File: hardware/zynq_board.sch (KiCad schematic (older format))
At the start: 0 parts

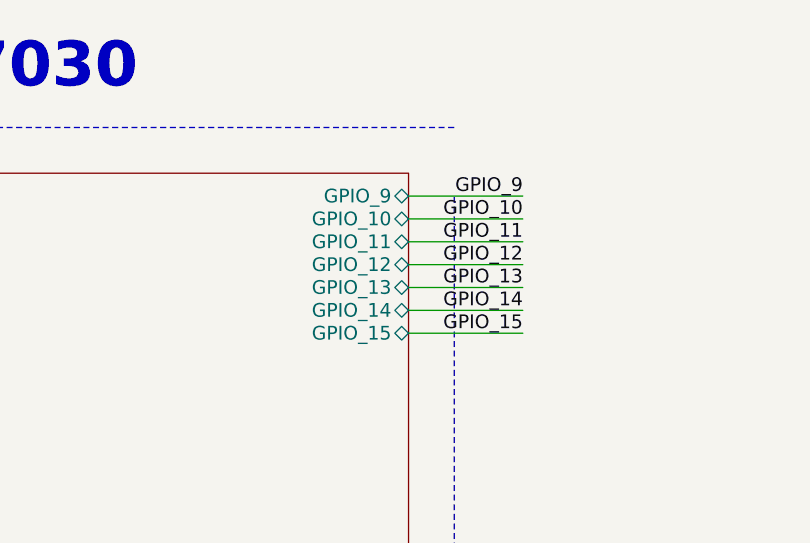
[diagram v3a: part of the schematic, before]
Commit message: general routing mainly power distribution, fixed some footprints
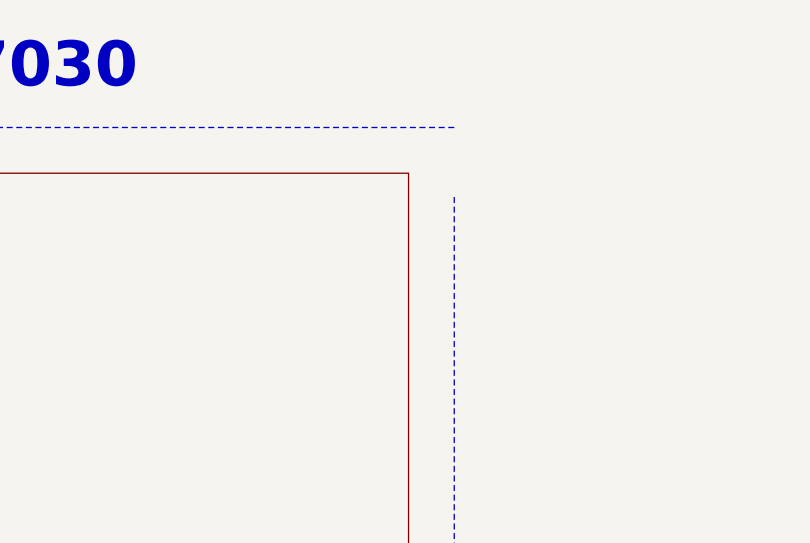
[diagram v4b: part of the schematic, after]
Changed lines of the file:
@@
 Text Label 17150 3800 2    60   ~ 0
 TRIG_IN_3
-Text Label 13750 3250 2    60   ~ 0
-GPIO_15
-Text Label 13750 3150 2    60   ~ 0
-GPIO_14
-Text Label 13750 3050 2    60   ~ 0
-GPIO_13
-Text Label 13750 2950 2    60   ~ 0
-GPIO_12
-Text Label 13750 2850 2    60   ~ 0
-GPIO_11
-Text Label 13750 2750 2    60   ~ 0
-GPIO_10
-Text Label 13750 2650 2    60   ~ 0
-GPIO_9
 Wire Notes Line
 	7250 2350 7250 21950
@@
 Wire Wire Line
 	16400 3800 17150 3800
-Wire Wire Line
-	13250 2650 13750 2650
-Wire Wire Line
-	13250 2750 13750 2750
-Wire Wire Line
-	13250 2850 13750 2850
-Wire Wire Line
-	13250 2950 13750 2950
-Wire Wire Line
-	13250 3050 13750 3050
-Wire Wire Line
-	13250 3150 13750 3150
-Wire Wire Line
-	13250 3250 13750 3250
 Text Label 13750 11150 2    60   ~ 0
 LED1
@@
 F0 "10G Clock" 60
 F1 "10G_clock.sch" 60
-$EndSheet
-$Sheet
-S 10500 2550 2750 3550
-U 596E75FA
-F0 "PL: Bank 34" 60
-F1 "zynq_pl_34.sch" 60
-F2 "SFP_GPIO_18" O R 13250 5400 60
-F3 "RX_LOS_18" I R 13250 5500 60
-F4 "MODDET_18" I R 13250 5600 60
-F5 "SFP_SDA_18" B R 13250 5700 60
-F6 "SFP_SCL_18" B R 13250 5800 60
-F7 "TX_FAULT_18" I R 13250 5900 60
-F8 "TX_DISABLE_18" O R 13250 6000 60
-F9 "ST" O R 13250 5100 60
-F10 "LS_OK_IN_A" O R 13250 5000 60
-F11 "LS_OK_OUT_A" I R 13250 4900 60
-F12 "PRBSEN" O R 13250 4800 60
-F13 "MDC" O R 13250 4700 60
-F14 "MDIO" B R 13250 4600 60
-F15 "GPIO_9" B R 13250 2650 60
-F16 "GPIO_10" B R 13250 2750 60
-F17 "GPIO_11" B R 13250 2850 60
-F18 "GPIO_12" B R 13250 2950 60
-F19 "GPIO_13" B R 13250 3050 60
-F20 "GPIO_14" B R 13250 3150 60
-F21 "GPIO_15" B R 13250 3250 60
 $EndSheet
 $Sheet
@@
 F2 "BUTTON1" O R 16700 9850 60
 $EndSheet
+$Sheet
+S 10500 2550 2750 3550
+U 596E75FA
+F0 "PL: Bank 34" 60
+F1 "zynq_pl_34.sch" 60
+F2 "SFP_GPIO_18" O R 13250 5400 60
+F3 "RX_LOS_18" I R 13250 5500 60
+F4 "MODDET_18" I R 13250 5600 60
+F5 "SFP_SDA_18" B R 13250 5700 60
+F6 "SFP_SCL_18" B R 13250 5800 60
+F7 "TX_FAULT_18" I R 13250 5900 60
+F8 "TX_DISABLE_18" O R 13250 6000 60
+F9 "ST" O R 13250 5100 60
+F10 "LS_OK_IN_A" O R 13250 5000 60
+F11 "LS_OK_OUT_A" I R 13250 4900 60
+F12 "PRBSEN" O R 13250 4800 60
+F13 "MDC" O R 13250 4700 60
+F14 "MDIO" B R 13250 4600 60
+$EndSheet
 $EndSCHEMATC

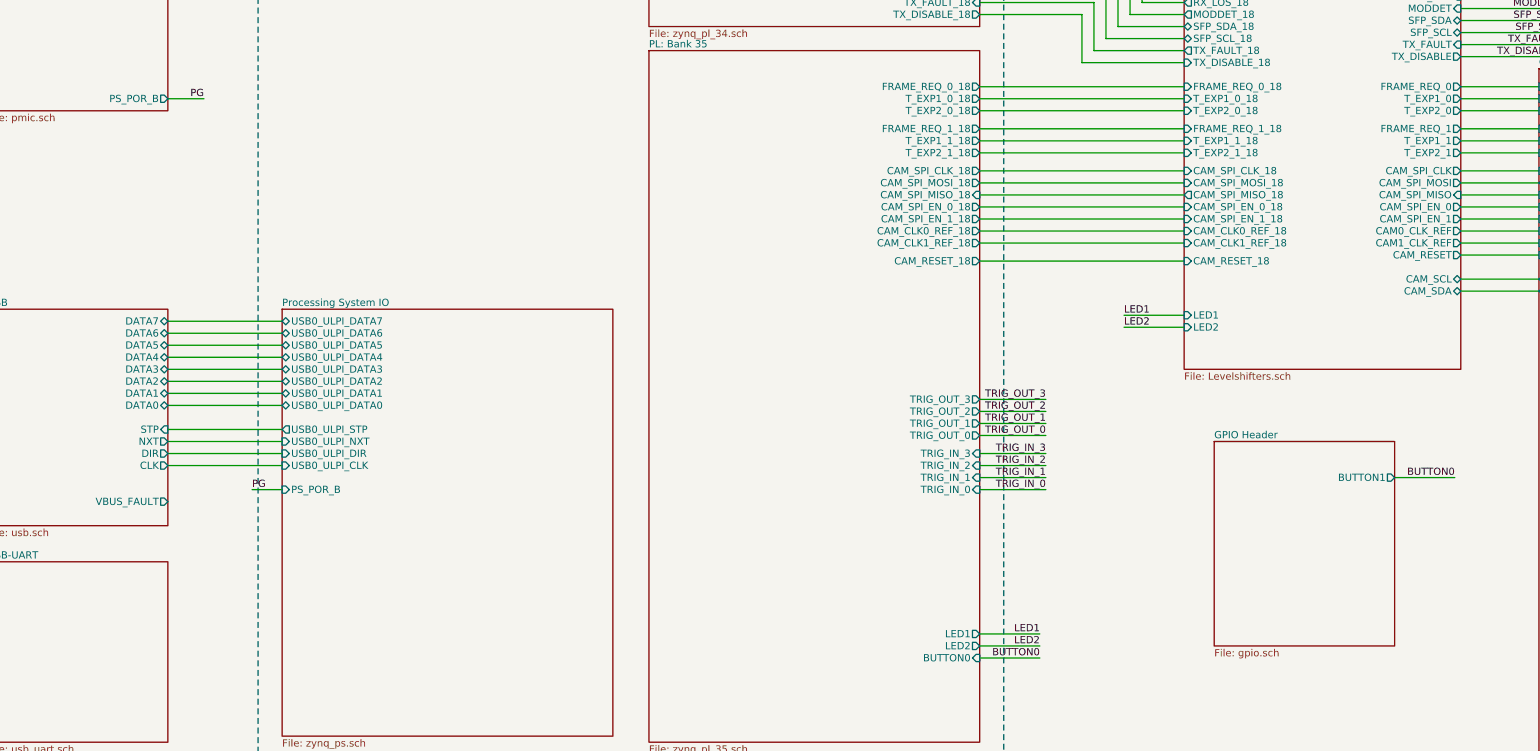
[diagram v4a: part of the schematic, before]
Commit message: First Version without any Net not routed.
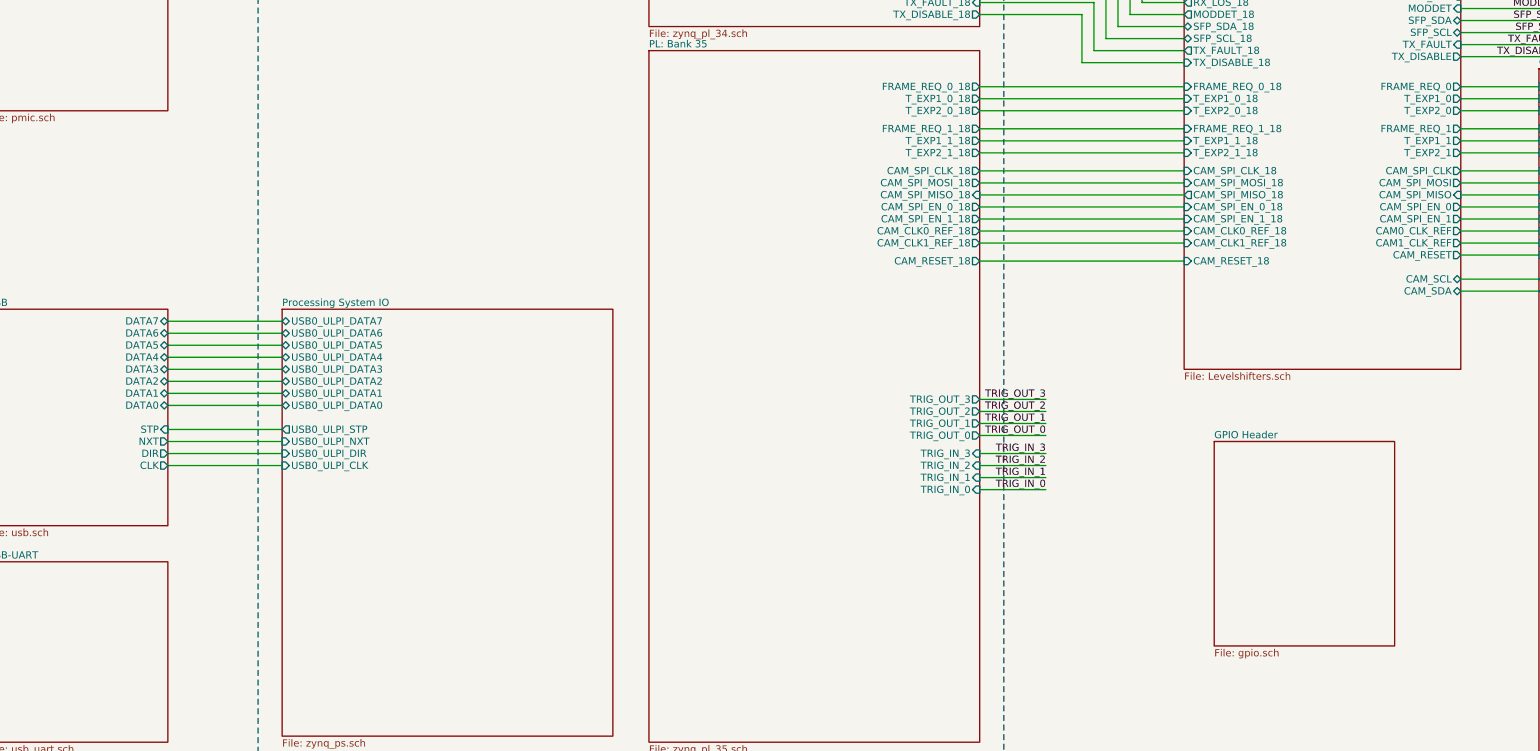
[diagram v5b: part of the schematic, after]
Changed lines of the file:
@@
 F0 "PMIC" 60
 F1 "pmic.sch" 60
-F2 "PS_POR_B" O R 6500 6700 60
 $EndSheet
 $Sheet
@@
 F0 "DDR" 60
 F1 "ddr.sch" 60
-$EndSheet
-$Sheet
-S 5000 8450 1500 1800
-U 5990E90D
-F0 "USB" 60
-F1 "usb.sch" 60
-F2 "DATA7" B R 6500 8550 60
-F3 "DATA6" B R 6500 8650 60
-F4 "DATA5" B R 6500 8750 60
-F5 "DATA4" B R 6500 8850 60
-F6 "DATA3" B R 6500 8950 60
-F7 "DATA2" B R 6500 9050 60
-F8 "DATA1" B R 6500 9150 60
-F9 "DATA0" B R 6500 9250 60
-F10 "STP" I R 6500 9450 60
-F11 "NXT" O R 6500 9550 60
-F12 "DIR" O R 6500 9650 60
-F13 "CLK" O R 6500 9750 60
-F14 "VBUS_FAULT" O R 6500 10050 60
 $EndSheet
 $Sheet
@@
 F44 "CAM_CLK0_REF_18" I L 14950 7800 60
 F45 "CAM0_CLK_REF" O R 17250 7800 60
-F46 "LED1" I L 14950 8500 60
-F47 "LED2" I L 14950 8600 60
 $EndSheet
 $Sheet
@@
 Wire Wire Line
 	16400 3800 17150 3800
-Text Label 13750 11150 2    60   ~ 0
-LED1
-Text Label 13750 11250 2    60   ~ 0
-LED2
-Text Label 13750 11350 2    60   ~ 0
-BUTTON0
-Wire Wire Line
-	13250 11150 13750 11150
-Wire Wire Line
-	13250 11250 13750 11250
-Wire Wire Line
-	13250 11350 13750 11350
-Text Label 17200 9850 2    60   ~ 0
-BUTTON0
-Wire Wire Line
-	16700 9850 17200 9850
-$Sheet
-S 7450 8450 2750 3550
-U 596E7567
-F0 "Processing System IO" 60
-F1 "zynq_ps.sch" 60
-F2 "USB0_ULPI_DATA0" B L 7450 9250 60
-F3 "USB0_ULPI_DATA1" B L 7450 9150 60
-F4 "USB0_ULPI_DATA2" B L 7450 9050 60
-F5 "USB0_ULPI_DATA3" B L 7450 8950 60
-F6 "USB0_ULPI_DATA5" B L 7450 8750 60
-F7 "USB0_ULPI_DATA6" B L 7450 8650 60
-F8 "USB0_ULPI_DATA7" B L 7450 8550 60
-F9 "USB0_ULPI_DATA4" B L 7450 8850 60
-F10 "USB0_ULPI_CLK" I L 7450 9750 60
-F11 "USB0_ULPI_DIR" I L 7450 9650 60
-F12 "USB0_ULPI_STP" O L 7450 9450 60
-F13 "USB0_ULPI_NXT" I L 7450 9550 60
-F14 "PS_POR_B" I L 7450 9950 60
-$EndSheet
 $Sheet
 S 5000 10550 1500 1500
@@
 Text Label 14100 4600 2    60   ~ 0
 MDIO
-Text Label 7200 9950 0    60   ~ 0
-PG
-Wire Wire Line
-	7450 9950 7200 9950
-Text Label 6800 6700 2    60   ~ 0
-PG
-Wire Wire Line
-	6800 6700 6500 6700
-Text Label 14450 8500 0    60   ~ 0
-LED1
-Text Label 14450 8600 0    60   ~ 0
-LED2
-Wire Wire Line
-	14950 8500 14450 8500
-Wire Wire Line
-	14950 8600 14450 8600
 $Sheet
 S 5000 3200 1500 1150
@@
 F20 "TRIG_OUT_1" O R 13250 9400 60
 F21 "TRIG_OUT_3" O R 13250 9200 60
-F22 "LED1" O R 13250 11150 60
-F23 "LED2" O R 13250 11250 60
-F24 "BUTTON0" I R 13250 11350 60
-F25 "CAM_CLK0_REF_18" O R 13250 7800 60
-F26 "CAM_CLK1_REF_18" O R 13250 7900 60
+F22 "CAM_CLK0_REF_18" O R 13250 7800 60
+F23 "CAM_CLK1_REF_18" O R 13250 7900 60
 $EndSheet
 $Sheet
@@
 F0 "GPIO Header" 60
 F1 "gpio.sch" 60
-F2 "BUTTON1" O R 16700 9850 60
 $EndSheet
 $Sheet
@@
 F14 "MDIO" B R 13250 4600 60
 $EndSheet
+$Sheet
+S 7450 8450 2750 3550
+U 596E7567
+F0 "Processing System IO" 60
+F1 "zynq_ps.sch" 60
+F2 "USB0_ULPI_DATA0" B L 7450 9250 60
+F3 "USB0_ULPI_DATA1" B L 7450 9150 60
+F4 "USB0_ULPI_DATA2" B L 7450 9050 60
+F5 "USB0_ULPI_DATA3" B L 7450 8950 60
+F6 "USB0_ULPI_DATA5" B L 7450 8750 60
+F7 "USB0_ULPI_DATA6" B L 7450 8650 60
+F8 "USB0_ULPI_DATA7" B L 7450 8550 60
+F9 "USB0_ULPI_DATA4" B L 7450 8850 60
+F10 "USB0_ULPI_CLK" I L 7450 9750 60
+F11 "USB0_ULPI_DIR" I L 7450 9650 60
+F12 "USB0_ULPI_STP" O L 7450 9450 60
+F13 "USB0_ULPI_NXT" I L 7450 9550 60
+$EndSheet
+$Sheet
+S 5000 8450 1500 1800
+U 5990E90D
+F0 "USB" 60
+F1 "usb.sch" 60
+F2 "DATA7" B R 6500 8550 60
+F3 "DATA6" B R 6500 8650 60
+F4 "DATA5" B R 6500 8750 60
+F5 "DATA4" B R 6500 8850 60
+F6 "DATA3" B R 6500 8950 60
+F7 "DATA2" B R 6500 9050 60
+F8 "DATA1" B R 6500 9150 60
+F9 "DATA0" B R 6500 9250 60
+F10 "STP" I R 6500 9450 60
+F11 "NXT" O R 6500 9550 60
+F12 "DIR" O R 6500 9650 60
+F13 "CLK" O R 6500 9750 60
+$EndSheet
 $EndSCHEMATC
